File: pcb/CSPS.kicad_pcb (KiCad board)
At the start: 2 copper layers, 95 x 40.6 mm, 43 parts, among them J1 Conn_02x32_Counter_Clockwise, J10 Conn_01x02, J11 Conn_01x02, J12 Conn_01x06, J13 Conn_01x06, J2 Conn_01x02, J3 Conn_01x03, J4 XT30, J5 XT30, J6 XT30, J7 XT30, J8 Conn_01x04, J9 Conn_01x02, Q1 AO3400A, Q2 AO3400A, SW1 SW_Push, U1 CH32V003AxMx, U2 TLV70433DBVR

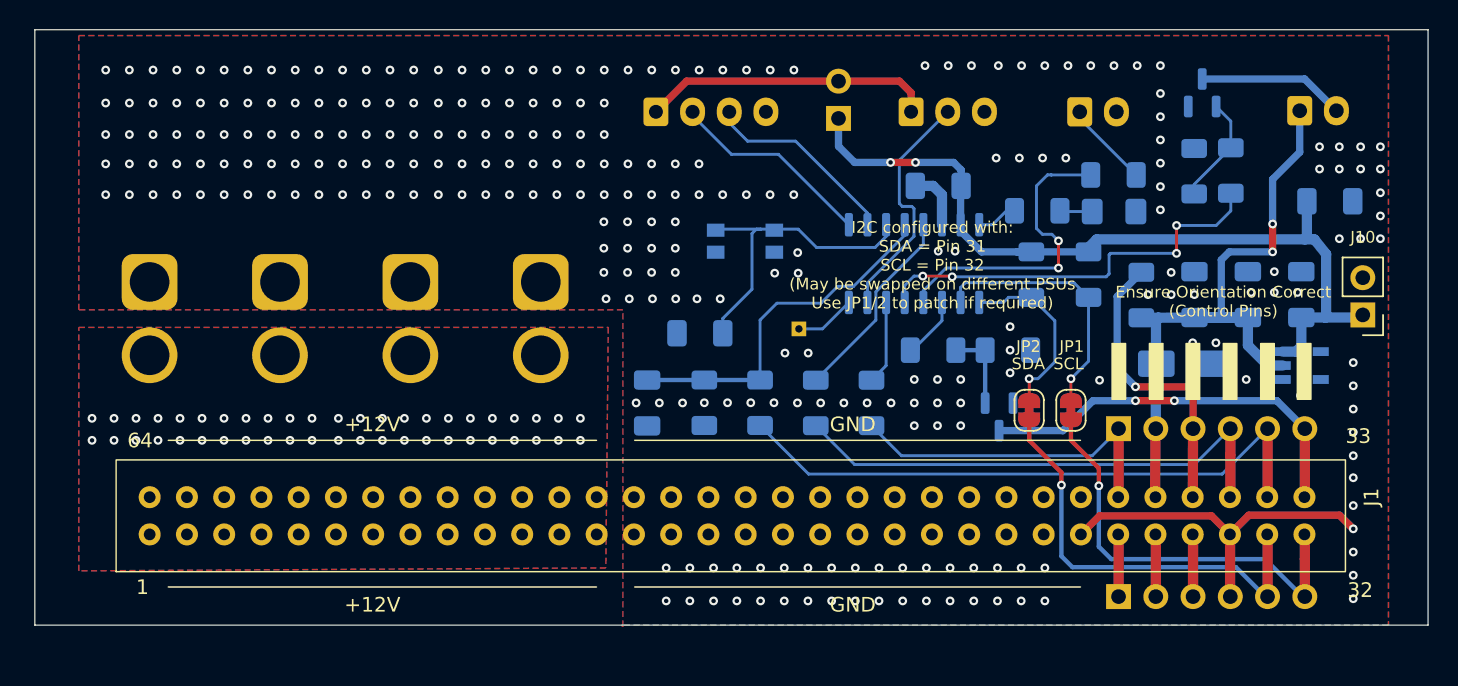
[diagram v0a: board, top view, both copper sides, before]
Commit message: Fix connector footprint
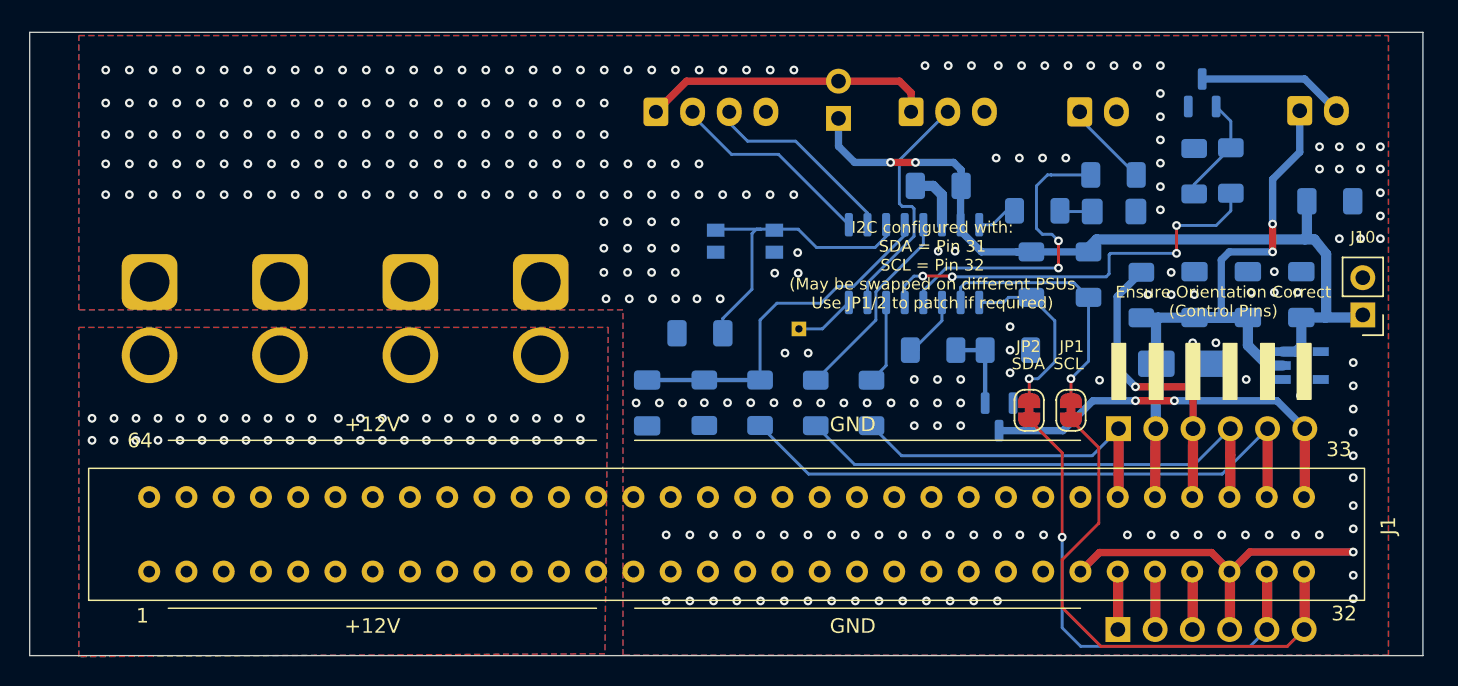
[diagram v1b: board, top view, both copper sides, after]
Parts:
- moved J12 2.25 mm to (192.8, 101.9)
- moved J1 1.95 mm to (205.8, 94.8)
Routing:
- net Net-(J1-Pin_32): track 29.4 -> 36.6 mm, vias 1 -> 0
- net Net-(J1-Pin_31): track 29.9 -> 34.2 mm
- net GND: track 37.9 -> 37.2 mm, vias 271 -> 278
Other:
- board size 95 x 40.6 mm -> 95 x 42.5 mm

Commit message: PCB Update
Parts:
- R6: value 22K -> 15K
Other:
- board text added: "Rev: 1.1 https://github.com/paulc/CSPS-Controller"
- board text removed: "Rev: 1.0 https://github.com/paulc/CSPS-Controller"
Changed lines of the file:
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@@
 			)
 		)
-		(attr through_hole exclude_from_pos_files exclude_from_bom)
+		(attr through_hole)
 		(duplicate_pad_numbers_are_jumpers no)
 		(fp_rect
@@
 			)
 		)
-		(property "LCSC" "C2907329"
+		(property "LCSC" "C4502"
 			(at 0 0 180)
 			(unlocked yes)
@@
 			)
 		)
-		(property "LCSC" "C2907423"
+		(property "LCSC" "C17902"
 			(at 0 0 90)
 			(unlocked yes)
@@
 			)
 		)
-		(property "LCSC" "C2907295"
+		(property "LCSC" "C4410"
 			(at 0 0 270)
 			(unlocked yes)
@@
 			)
 		)
-		(property "LCSC" "C2907423"
+		(property "LCSC" "C17902"
 			(at 0 0 90)
 			(unlocked yes)
@@
 			)
 		)
-		(property "LCSC" "C105427"
+		(property "LCSC" "C17936"
 			(at 0 0 270)
 			(unlocked yes)
@@
 			)
 		)
-		(property "LCSC" "C126469"
+		(property "LCSC" "C24497"
 			(at 0 0 270)
 			(unlocked yes)
@@
 			)
 		)
-		(property "Value" "22K"
+		(property "Value" "15K"
 			(at 0 -1.83 90)
 			(layer "B.Fab")
@@
 			)
 		)
-		(property "LCSC" "C2907309"
+		(property "LCSC" "C25828"
 			(at 0 0 270)
 			(unlocked yes)
@@
 			)
 		)
-		(property "LCSC" "C98192"
+		(property "LCSC" "C29823"
 			(at 0 0 270)
 			(unlocked yes)
@@
 		(tags "Diode SMA (DO-214AC)")
 		(property "Reference" "D3"
-			(at -4.57 0.825 0)
+			(at -5.27 0.045 0)
 			(layer "B.SilkS")
 			(effects
@@
 			)
 		)
-		(property "LCSC" "C965815"
+		(property "LCSC" "C3646937"
 			(at 0 0 0)
 			(unlocked yes)
@@
 			)
 		)
-		(property "LCSC" "C114237"
+		(property "LCSC" "C17948"
 			(at 0 0 90)
 			(unlocked yes)
@@
 			)
 		)
-		(property "LCSC" "C2907423"
+		(property "LCSC" "C17902"
 			(at 0 0 90)
 			(unlocked yes)
@@
 			)
 		)
-		(property "LCSC" "C2907294"
+		(property "LCSC" "C17901"
 			(at 0 0 180)
 			(unlocked yes)
@@
 			)
 		)
-		(property "LCSC" "C126469"
+		(property "LCSC" "C24497"
 			(at 0 0 0)
 			(unlocked yes)
@@
 			)
 		)
-		(property "LCSC" "C2907294"
+		(property "LCSC" "C17901"
 			(at 0 0 270)
 			(unlocked yes)
@@
 			)
 		)
-		(property "LCSC" "C126469"
+		(property "LCSC" "C24497"
 			(at 0 0 180)
 			(unlocked yes)
@@
 			)
 		)
-		(property "LCSC" "C114237"
+		(property "LCSC" "C17948"
 			(at 0 0 90)
 			(unlocked yes)
@@
 			)
 		)
-		(property "LCSC" "C2907294"
+		(property "LCSC" "C17901"
 			(at 0 0 180)
 			(unlocked yes)
@@
 			)
 		)
-		(property "LCSC" "C2907423"
+		(property "LCSC" "C17902"
 			(at 0 0 0)
 			(unlocked yes)
@@
 			)
 		)
-		(property "LCSC" "C126469"
+		(property "LCSC" "C24497"
 			(at 0 0 0)
 			(unlocked yes)
@@
 			)
 		)
-		(property "LCSC" "C19110"
+		(property "LCSC" "C50254"
 			(at 0 0 270)
 			(unlocked yes)
@@
 			)
 		)
-		(property "LCSC" "C126469"
+		(property "LCSC" "C24497"
 			(at 0 0 90)
 			(unlocked yes)
@@
 		(layer "B.SilkS")
 	)
+	(gr_line
+		(start 193.5 82.2)
+		(end 193.5 85.4)
+		(stroke
+			(width 0.25)
+			(type solid)
+		)
+		(layer "B.SilkS")
+	)
+	(gr_line
+		(start 197 83)
+		(end 197 84.6)
+		(stroke
+			(width 0.1)
+			(type default)
+		)
+		(layer "B.SilkS")
+	)
+	(gr_line
+		(start 197.8 83)
+		(end 197 83.8)
+		(stroke
+			(width 0.1)
+			(type default)
+		)
+		(layer "B.SilkS")
+	)
+	(gr_line
+		(start 197.8 83)
+		(end 197.8 84.6)
+		(stroke
+			(width 0.1)
+			(type default)
+		)
+		(layer "B.SilkS")
+	)
+	(gr_line
+		(start 197.8 84.6)
+		(end 197 83.8)
+		(stroke
+			(width 0.1)
+			(type default)
+		)
+		(layer "B.SilkS")
+	)
 	(gr_rect
 		(start 118.65 61.179518)
@@
 		)
 	)
-	(gr_text "Rev: 1.0  https://github.com/paulc/CSPS-Controller"
+	(gr_text "Rev: 1.1  https://github.com/paulc/CSPS-Controller"
 		(at 157.4 66.75 0)
 		(layer "B.SilkS")
@@
 		(layer "B.SilkS")
 		(effects
-			(font
-				(size 1 1)
-				(thickness 0.1)
-			)
-			(justify left bottom mirror)
-		)
-	)
-	(gr_text "+"
-		(at 193.7 83.7 0)
-		(layer "B.SilkS")
-		(effects
